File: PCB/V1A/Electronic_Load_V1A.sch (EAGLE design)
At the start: 231 parts, among them IC201 MAX743CPE, IC202 7805T, IC203 7805T, IC204 7905, IC205 LM50, IC206 LM50, IC301 OPA77P, IC401 AD620R, IC402 AD620R, IC403 AD620R, IC404 AD620R, IC405 LM50, IC406 LM50, IC407 AD620R, J101 +, J102 -, J103 +, J104 -, Q1 BC807-16SMD, Q101 SIRC10DP, Q102 SIRC10DP, Q103 SIRC10DP, Q104 IXTK102N65X2PADUP, Q105 SIRC10DP, Q106 SIRC10DP, Q107 SIRC10DP, Q108 IXTK102N65X2PADUP, Q2 BC807-16SMD, Q3 BC807-16SMD, Q301 BC817-25SMD, Q302 BC807-25SMD, Q303 BC817-25SMD, Q4 BC807-16SMD, Q5 BC807-16SMD, Q501 BC807-16SMD, Q502 BC807-16SMD, Q503 BC807-16SMD, Q504 BC807-16SMD, Q505 BC807-16SMD, Q506 BC807-16SMD, Q6 BC807-16SMD, U1 HCPL-063N, U2 HCPL-063N, U3 HCPL-063N, U301 AD420, U302 AD420, U303 LT1014, U401 LTC1865L, U402 LTC1865L, U403 LTC1865L, U404 LTC1865L, U501 HCPL-063N, U502 HCPL-063N, U503 HCPL-063N

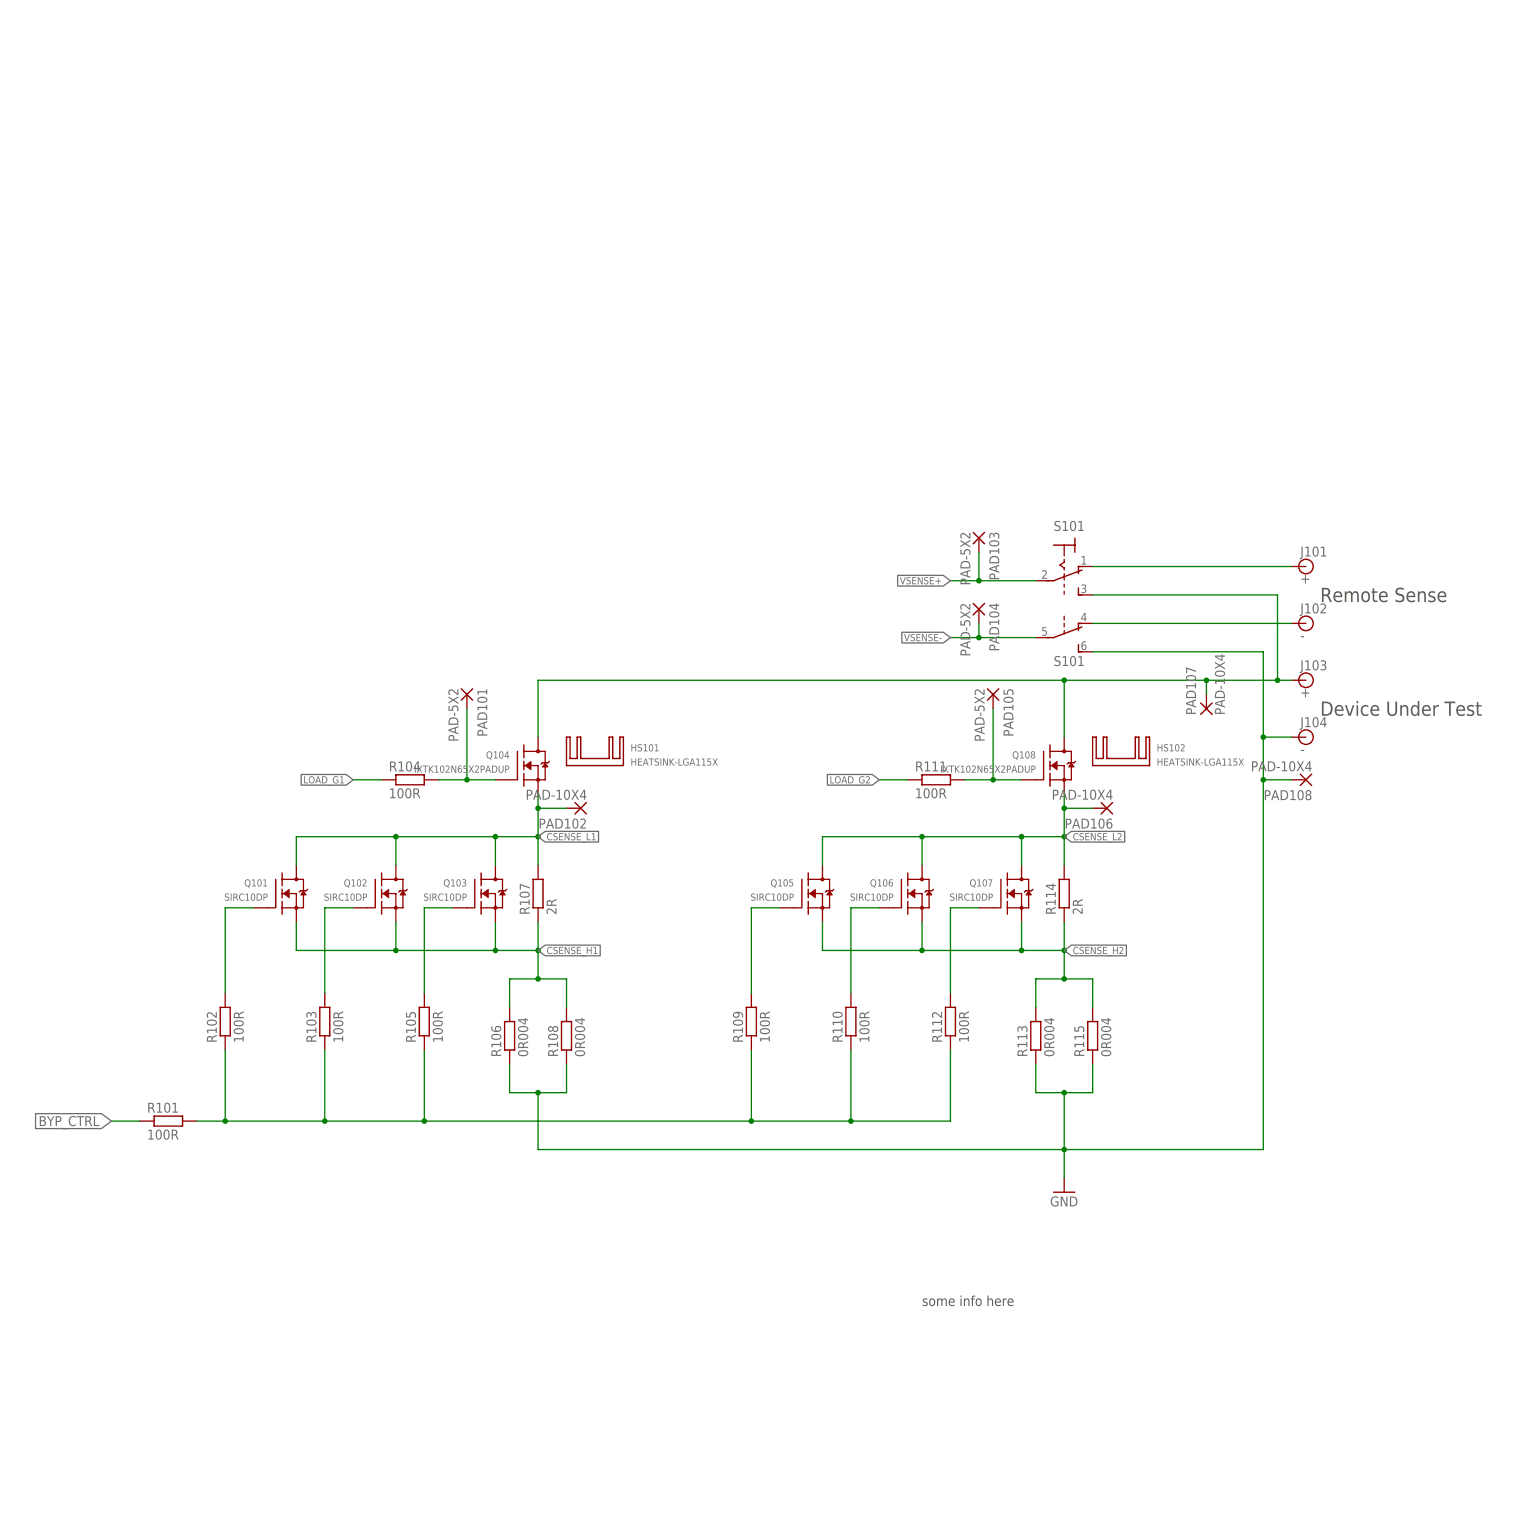
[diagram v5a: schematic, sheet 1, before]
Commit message: Removed board layout, updated schematic layout
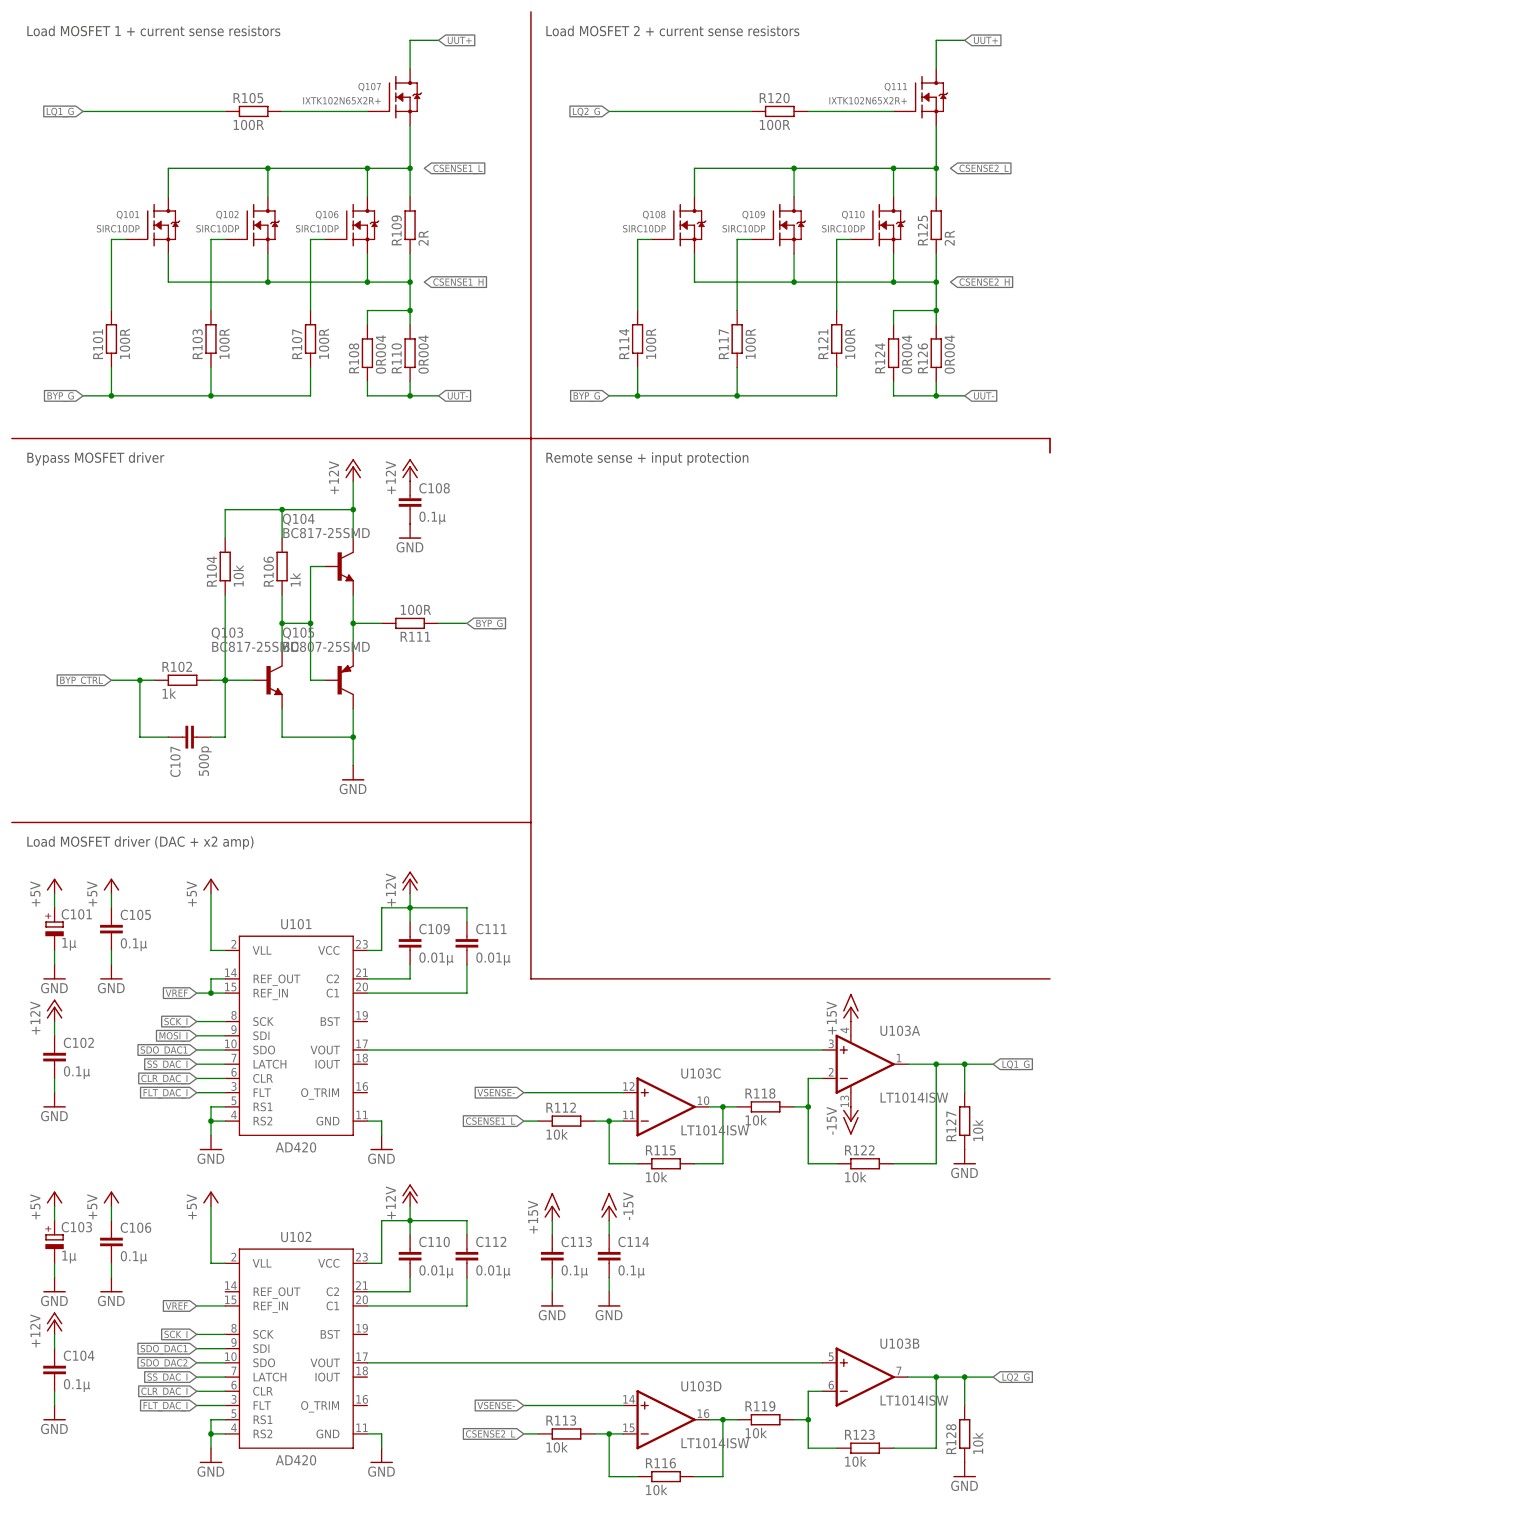
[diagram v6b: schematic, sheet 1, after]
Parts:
- removed C1, C301, C302, C303, C309, C311, C312, C5, C9: 0.1µ, rcl:C-EUC1206
- removed C10, C2, C6: 0.01µ, rcl:C-EUC1206
- removed C11, C12, C3, C4, C7, C8: 15p, rcl:C-EUC1206
- removed C13, C14, C15, C16, C308: 500p, rcl:C-EUC1206
- removed C304, C305, C306, C307: 10n, rcl:C-EUC0805
- removed C310: 0.1µ, rcl:C-EUC0805
- removed HS101, HS102: HEATSINK-LGA115X, mechanical:HEATSINK-LGA115X
- removed J101, J103: +, SparkFun-Connectors:BANANA_CONN
- removed J102, J104: -, SparkFun-Connectors:BANANA_CONN
- removed PAD101, PAD103, PAD104, PAD105: PAD-5X2, pads:PAD-5X2
- removed PAD102, PAD106, PAD107, PAD108: PAD-10X4, pads:PAD-10X4
- removed Q1, Q2, Q3, Q4, Q5, Q6: BC807-16SMD, transistor-pnp:BC807-16SMD
- removed Q301, Q303: BC817-25SMD, transistor-npn:BC817-25SMD
- removed Q302: BC807-25SMD, transistor-pnp:BC807-25SMD
- removed R1, R10, R11, R12, R2, R3, R4, R5, R6, R7, R8, R9: 350R, rcl:R-EU_R1206
- removed R13, R14, R15, R16, R309, R310: 100R, rcl:R-EU_R1206
- removed R301, R303: 1k, rcl:R-EU_R0603
- removed R302, R304: 10k, rcl:R-EU_R0603
- removed R305, R306: 20k, rcl:R-TRIMM4G/J
- removed R307, R308: 200k, rcl:R-EU_R1206
- removed R311, R312, R313, R314: 5k, rcl:R-EU_R0603
- removed S101: (no value), switch:320-938
- removed U1, U2, U3: HCPL-063N, isolation:HCPL-063N
- removed U301, U302: AD420, adc_dac:AD420
- removed U303: LT1014, SparkFun-Retired:LT1014
- added C101, C103, C426, C427: 1µ, rcl:CPOL-EUSMCA
- added C102, C104, C105, C106, C108, C113, C114, C428, C429, C513, C514, C515: 0.1µ, rcl:C-EUC1206
- added C107: 500p, rcl:C-EUC1206
- added C109, C110, C111, C112, C516, C517, C518: 0.01µ, rcl:C-EUC1206
- added C519, C520, C521, C522, C523, C524: 15p, rcl:C-EUC1206
- added Q109, Q110: SIRC10DP, transistors:SIRC10DP
- added Q111: IXTK102N65X2R+, transistors:IXTK102N65X2R+
- added Q507, Q508, Q509, Q510, Q511, Q512: BC807-16SMD, transistor-pnp:BC807-16SMD
- added R116, R118, R119, R122, R123, R127, R128: 10k, rcl:R-EU_R0603
- added R117, R120, R121: 100R, rcl:R-EU_R1206
- added R124, R126: 0R004, rcl:R-EU_R6332
- added R125: 2R, rcl:R-EU_R1206
- added R412, R413: 2M, rcl:R-EU_R1206
- added R414, R415: 2k15, rcl:R-EU_R1206
- added R513, R514, R515, R516, R517, R518, R519, R520, R521, R522, R523, R524: 350R, rcl:R-EU_R1206
- added U101, U102: AD420, adc_dac:AD420RW-24
- added U103: LT1014ISW, ic:LT1014ISW
- added U504, U505, U506: HCPL-063N, isolation:HCPL-063N
- C409, C410: value 1µ -> 500p; device rcl:CPOL-EUSMCA -> rcl:C-EUC1206
- C411, C412: value 0.1µ -> 500p
- C413, C414, C421, C422: value 0.1µ -> 1µ; device rcl:C-EUC1206 -> rcl:CPOL-EUSMCA
- C417, C418, C419, C420: value 1µ -> 0.1µ; device rcl:CPOL-EUSMCA -> rcl:C-EUC1206
- Q103: value SIRC10DP -> BC817-25SMD; device transistors:SIRC10DP -> transistor-npn:BC817-25SMD
- Q104: value IXTK102N65X2PADUP -> BC817-25SMD; device transistors:IXTK102N65X2PADUP -> transistor-npn:BC817-25SMD
- Q105: value SIRC10DP -> BC807-25SMD; device transistors:SIRC10DP -> transistor-pnp:BC807-25SMD
- Q107: value SIRC10DP -> IXTK102N65X2R+; device transistors:SIRC10DP -> transistors:IXTK102N65X2R+
- Q108: value IXTK102N65X2PADUP -> SIRC10DP; device transistors:IXTK102N65X2PADUP -> transistors:SIRC10DP
- R102: value 100R -> 1k; device rcl:R-EU_R1206 -> rcl:R-EU_R0603
- R104, R112: value 100R -> 10k; device rcl:R-EU_R1206 -> rcl:R-EU_R0603
- R106: value 0R004 -> 1k; device rcl:R-EU_R6332 -> rcl:R-EU_R0603
- R107, R114: value 2R -> 100R
- R109: value 100R -> 2R
- R110: value 100R -> 0R004; device rcl:R-EU_R1206 -> rcl:R-EU_R6332
- R113, R115: value 0R004 -> 10k; device rcl:R-EU_R6332 -> rcl:R-EU_R0603
- R405, R406, R407, R408: value 2M -> 100R
- R410, R411: value 2k15 -> 2M
- renumbered C17 to C423, C18 to C425, C19 to C424, R17 to R416, R18 to R418, R19 to R417
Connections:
- net N$56 renamed LBQ12_G
- removed net DAC1_OUT: U301.DATA_OUT, U302.DATA_IN
- removed net DAC2_OUT: U302.DATA_OUT
- removed net DUT_+1: J103.1, PAD107.P, Q104.D, Q108.D, S1011.S
- removed net LOAD_G1: R104.1, R313.2, U303G1.OUT
- removed net LOAD_G2: R111.1, R314.2, U303G2.OUT
- removed net N$24: C307.1, U302.CAP2
- removed net N$25: C304.1, U301.CAP1
- removed net N$26: C305.1, U302.CAP1
- removed net N$27: C306.1, U301.CAP2
- removed net N$28: R311.2, R313.1, U303G1.-IN
- removed net N$29: R312.2, R314.1, U303G2.-IN
- removed net N$32: R307.2, R309.2, R311.1
- removed net N$33: R305.S, R307.1
- removed net N$34: R306.S, R308.1
- removed net N$35: R308.2, R310.2, R312.1
- removed net N$52: PAD101.P, Q104.G, R104.2
- removed net N$54: PAD105.P, Q108.G, R111.2
- removed net N$55: Q103.G, R105.2
- removed net N$57: Q107.G, R112.2
- removed net N$58: Q106.G, R110.2
- removed net N$59: R101.2, R102.1, R103.1, R105.1, R109.1, R110.1, R112.1
- removed net N$60: Q101.G, R102.2
- removed net N$61: Q105.G, R109.2
- removed net N$66 (its old number): Q1.E, R3.1, U1.A1
- removed net N$67 (its old number): Q2.E, R4.1, U1.A2
- removed net N$68 (its old number): Q5.E, R11.1, U3.A1
- removed net N$69 (its old number): Q6.E, R12.1, U3.A2
- removed net N$76 (its old number): Q3.E, R7.1, U2.A1
- removed net N$77 (its old number): Q4.E, R8.1, U2.A2
- removed net N$93: Q301.B, Q302.B, Q303.C, R301.1
- removed net N$94: C303.1, Q301.C, R301.2, R302.2
- removed net N$95: C303.2, Q302.C, Q303.E
- removed net N$96: C308.1, Q303.B, R302.1, R303.2
- removed net REM_VSENSE+1: J101.1, S1011.O
- removed net REM_VSENSE-1: J102.1, S101B.O
- removed net VGATE_1: U301.VOUT, U303G1.+IN
- removed net VGATE_2: U302.VOUT, U303G2.+IN
- new net BYP_G_LOL: Q504.B
- new net CLR_DAC_I: U101.CLR, U102.CLR
- new net CSENSE1_H: Q101.S, Q102.S, Q106.S, R108.2, R109.1, R110.2
- new net CSENSE1_L: Q101.D, Q102.D, Q106.D, Q107.S, R109.2, R112.1
- new net CSENSE2_H: Q108.S, Q109.S, Q110.S, R124.2, R125.1, R126.2
- new net CSENSE2_L: Q108.D, Q109.D, Q110.D, Q111.S, R113.1, R125.2
- new net FLT_DAC_I: U101.FLT, U102.FLT
- new net LBQ11_G: Q101.G, R101.2
- new net LBQ13_G: Q106.G, R107.2
- new net LBQ21_G: Q108.G, R114.2
- new net LBQ22_G: Q109.G, R117.2
- new net LBQ23_G: Q110.G, R121.2
- new net LQ1_G: R105.1, R122.2, R127.2, U103A.OUT
- new net LQ2_G: R120.1, R123.2, R128.2, U103B.OUT
- new net MOSI_I: U101.SDI
- new net N$1: Q107.G, R105.2
- new net N$10: U101.VOUT, U103A.+IN
- new net N$11: U102.VOUT, U103B.+IN
- new net N$12: R118.2, R122.1, U103A.-IN
- new net N$13: R115.2, R118.1, U103C.OUT
- new net N$14: R112.2, R115.1, U103C.-IN
- new net N$15: R113.2, R116.1, U103D.-IN
- new net N$16: R116.2, R119.1, U103D.OUT
- new net N$2: Q111.G, R120.2
- new net N$3: C109.2, U101.C2
- new net N$4: C111.2, U101.C1
- new net N$47: Q507.E, R513.1, U504.A1
- new net N$49: Q508.E, R514.1, U505.A1
- new net N$5: Q103.C, Q104.B, Q105.B, R106.1
- new net N$6: C110.2, U102.C2
- new net N$62: Q510.E, R516.1, U504.A2
- new net N$63: Q511.E, R517.1, U505.A2
- new net N$64: Q509.E, R515.1, U506.A1
- new net N$65: Q512.E, R518.1, U506.A2
- new net N$7: C112.2, U102.C1
- new net N$8: C107.2, Q103.B, R102.2, R104.1
- new net N$9: R119.2, R123.1, U103B.-IN
- new net SCK_I: U101.SCK, U102.SCK
- new net SDO_DAC1: U101.SDO, U102.SDI
- new net SDO_DAC2: U102.SDO
- new net SS_DAC_I: U101.LATCH, U102.LATCH
- new net UUT+: Q107.D, Q111.D
- new net UUT-: R108.1, R110.1, R124.1, R126.1
- net +12V: now also C102.1, C104.1, C108.1, C109.1, C110.1, C111.1, C112.1, Q104.C, R104.2, R106.2, U101.VCC, U102.VCC; no longer C304.2, C305.2, C306.2, C307.2, C309.1, C310.1, U301.VCC, U302.VCC
- net +15V: now also C113.1, C419.1, U103A.V+; no longer C311.1, C415.1, U303G1.+V
- net +3V3: now also C413.+, C414.+, C415.1, C416.1, C426.+, C427.+, C428.1, C429.1; no longer C409.+, C410.+, C411.1, C412.1, C419.+, C420.+, C421.1, C422.1
- net +5V: now also C101.+, C103.+, C105.1, C106.1, C417.1, C418.1, C513.1, C514.1, C515.1, C516.1, C517.1, C518.1, R513.2, R514.2, R515.2, R516.2, R517.2, R518.2, R519.2, R520.2, R521.2, R522.2, R523.2, R524.2, U101.VLL, U102.VLL, U504.VCC, U505.VCC, U506.VCC; no longer C1.1, C10.1, C2.1, C301.1, C302.1, C413.1, C414.1, C5.1, C6.1, C9.1, R1.2, R10.2, R11.2, R12.2, R2.2, R3.2, R304.2, R4.2, R5.2, R6.2, R7.2, R8.2, R9.2, U1.VCC, U2.VCC, U3.VCC, U301.VLL, U302.VLL
- net +5V/1: no longer R305.E, R306.E
- net -15V: now also C114.1, C420.1, U103A.V-; no longer C312.1, C416.1, U303G1.-V
- net -5V: no longer R305.A, R306.A
- net BYP_CTRL: now also C107.1, R102.1; no longer C308.2, R101.1, R303.1
- net BYP_G: now also R101.1, R103.1, R107.1, R111.1, R114.1, R117.1, R121.1; no longer Q4.B
- net BYP_G_ISO: now also C510.1, Q104.E, Q105.E, R111.2, R510.1, U501.VO2; no longer C8.1, Q301.E, Q302.E, R6.1, U2.VO2
- net CSENSE_H1: no longer Q101.S, Q102.S, Q103.S, R106.2, R107.1, R108.2
- net CSENSE_H2: no longer Q105.S, Q106.S, Q107.S, R113.2, R114.1, R115.2
- net CSENSE_L1: no longer PAD102.P, Q101.D, Q102.D, Q103.D, Q104.S, R107.2
- net CSENSE_L2: no longer PAD106.P, Q105.D, Q106.D, Q107.D, Q108.S, R114.2
- net DAC_CLR: now also Q503.B; no longer Q5.B
- net DAC_CLR_ISO: now also C509.1, R509.1, U503.VO1; no longer C11.1, R9.1, U3.VO1
- net DAC_FAULT: now also C511.1, R511.1, U502.VO2; no longer C4.1, R2.1, U1.VO2
- net DAC_FAULT_ISO: now also Q505.B; no longer Q2.B, R304.1, U301.FAULT, U302.FAULT
- net GND: now also C101.-, C102.2, C103.-, C104.2, C105.2, C106.2, C108.2, C113.2, C114.2, C409.2, C410.2, C413.-, C414.-, C417.2, C418.2, C419.2, C420.2, C421.-, C422.-, C426.-, C427.-, C428.2, C429.2, C513.2, C514.2, C515.2, C516.2, C517.2, C518.2, C519.2, C520.2, C521.2, C522.2, C523.2, C524.2, Q103.E, Q105.C, Q507.C, Q508.C, Q509.C, Q510.C, Q511.C, Q512.C, R127.1, R128.1, R414.1, U101.GND, U101.RS1, U101.RS2, U102.GND, U102.RS1, U102.RS2, U504.C1, U504.C2, U504.GND, U505.C1, U505.C2, U505.GND, U506.C1, U506.C2, U506.GND; no longer C1.2, C10.2, C11.2, C12.2, C13.2, C14.2, C15.2, C16.2, C2.2, C3.2, C301.2, C302.2, C309.2, C310.2, C311.2, C312.2, C4.2, C409.-, C410.-, C413.2, C414.2, C417.-, C418.-, C419.-, C420.-, C421.2, C422.2, C5.2, C6.2, C7.2, C8.2, C9.2, J104.1, PAD108.P, Q1.C, Q2.C, Q3.C, Q4.C, Q5.C, Q6.C, R106.1, R108.1, R113.1, R115.1, R309.1, R310.1, R410.1, S101B.S, U1.C1, U1.C2, U1.GND, U2.C1, U2.C2, U2.GND, U3.C1, U3.C2, U3.GND, U301.GND, U301.RS1, U301.RS2, U302.GND, U302.RS1, U302.RS2
- net MISO: now also C508.1, R508.1, U502.VO1; no longer C3.1, R1.1, U1.VO1
- net MISO_ISO: now also Q502.B; no longer Q1.B
- net MOSI: now also Q510.B; no longer Q504.B, U301.DATA_IN
- net MOSI_ISO: now also C522.1, R522.1, U504.VO2; no longer C510.1, R510.1, U501.VO2
- net N$100: now also R412.1, R413.2; no longer R408.1, R409.2
- net N$101: now also R413.1, R414.2; no longer R409.1, R410.2
- net N$70: now also R405.1; no longer R13.1
- net N$71: now also Q506.B; no longer Q6.B
- net N$72: now also C409.1, R405.2; no longer C13.1, R13.2
- net N$73: now also C512.1, R512.1, U503.VO2; no longer C12.1, R10.1, U3.VO2
- net N$74: now also R406.1; no longer R14.1
- net N$75: now also C410.1, R406.2; no longer C14.1, R14.2
- net N$78: now also C411.1, R407.2; no longer C15.1, R15.2
- net N$79: now also C412.1, R408.2; no longer C16.1, R16.2
- net N$80: now also R408.1; no longer R16.1
- net N$81: now also R407.1; no longer R15.1
- net N$97: now also R409.2, R411.1; no longer R405.2, R407.1
- net N$98: now also R410.1, R411.2; no longer R406.1, R407.2
- net N$99: now also R410.2, R412.2; no longer R406.2, R408.2
- net RG1_H3: now also R415.2; no longer R411.2
- net RG2_H3: now also R415.1; no longer R411.1
- net SCK: now also Q507.B; no longer Q501.B, U301.CLOCK, U302.CLOCK
- net SCK_ISO: now also C519.1, R519.1, U504.VO1; no longer C507.1, R507.1, U501.VO1
- net SS_CH: now also Q508.B; no longer Q502.B
- net SS_CH_ISO: now also C520.1, R520.1, U505.VO1; no longer C508.1, R508.1, U502.VO1
- net SS_CL: now also Q511.B; no longer Q505.B
- net SS_CL_ISO: now also C523.1, R523.1, U505.VO2; no longer C511.1, R511.1, U502.VO2
- net SS_DAC: now also Q501.B; no longer Q3.B
- net SS_DAC_ISO: now also C507.1, R507.1, U501.VO1; no longer C7.1, R5.1, U2.VO1
- net SS_TEMP: now also Q512.B; no longer Q506.B
- net SS_TEMP_ISO: now also C524.1, R524.1, U506.VO2; no longer C512.1, R512.1, U503.VO2
- net SS_V: now also Q509.B; no longer Q503.B
- net SS_V_ISO: now also C521.1, R521.1, U506.VO1; no longer C509.1, R509.1, U503.VO1
- net TEMP1: now also C421.+; no longer C417.+
- net TEMP2: now also C422.+; no longer C418.+
- net VREF: now also U101.REF_IN, U101.REF_OUT, U102.REF_IN; no longer U301.REF_IN, U301.REF_OUT, U302.REF_IN
- net VSENSE+: now also R409.1; no longer PAD103.P, R405.1, S1011.P
- net VSENSE-: now also U103C.+IN, U103D.+IN; no longer PAD104.P, S101B.P
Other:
- note added: "Bypass MOSFET driver"
- note added: "Load MOSFET 1 + current sense resistors"
- note added: "Load MOSFET 2 + current sense resistors"
- note added: "Load MOSFET driver (DAC + x2 amp)"
- note added: "Remote sense + input protection"
- note removed: "Device Under Test"
- note removed: "Remote Sense"
- moved on the sheet: C411, C412, C415, C416, C501, C502, C503, C504, C505, C506, C507, C508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

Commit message: Schematic & layout work; added block diagram
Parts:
- removed C314, C401, C402, C403, C404, C405, C406, C407, C408, C415, C416, C417, C418, C419, C420, C428, C429, C501, C502, C503, C513, C514, C515: 0.1µ, rcl:C-EUC1206
- removed C409, C410, C411, C412, C423, C424, C425: 500p, rcl:C-EUC1206
- removed C413, C414, C421, C422, C426, C427: 1µ, rcl:CPOL-EUSMCA
- removed C504, C505, C506, C516, C517, C518: 0.01µ, rcl:C-EUC1206
- removed C507, C508, C509, C510, C511, C512, C519, C520, C521, C522, C523, C524: 15p, rcl:C-EUC1206
- removed D201, D202: 1N5817-B, diode:1N5817-B
- removed D203, D204: 1N4004, diode:1N4004
- removed IC201: MAX743CPE, maxim:MAX743CPE
- removed IC202, IC203: 7805T, linear:7805T
- removed IC204: 7905, linear:7905T
- removed IC205, IC206, IC405, IC406: LM50, linear:LM50
- removed IC401, IC402, IC403, IC404, IC407: AD620R, analog-devices:AD620R
- removed J201: (no value), con-jack:JACK-PLUG0
- removed L201, L202: 100µ, rcl:L-EU0204/5
- removed Q501, Q502, Q503, Q504, Q505, Q506, Q507, Q508, Q509, Q510, Q511, Q512: BC807-16SMD, transistor-pnp:BC807-16SMD
- removed R315, R316, R317, R318: 20k, rcl:R-EU_R0603
- removed R319: 20k, rcl:R-TRIMM4G/J
- removed R401, R402, R403, R404, R414, R415: 2k15, rcl:R-EU_R1206
- removed R405, R406, R407, R408, R416, R417, R418: 100R, rcl:R-EU_R1206
- removed R409, R410, R411, R412, R413: 2M, rcl:R-EU_R1206
- removed R501, R502, R503, R504, R505, R506, R507, R508, R509, R510, R511, R512, R513, R514, R515, R516, R517, R518, R519, R520, R521, R522, R523, R524: 350R, rcl:R-EU_R1206
- removed U401, U402, U403, U404: LTC1865L, adc_dac:LTC1865L
- removed U501, U502, U503, U504, U505, U506: HCPL-063N, isolation:HCPL-063N
- added C115, C116, C118, C217, C218, C219, C221, C301, C311, C312, C601, C602, C603, C613, C614, C615: 0.1µ, passives:C-EU-3216
- added C117, C119, C120, C220, C302: 1µ, passives:CPOL-3216-A
- added C121, C122: 500p, passives:C-EU-3216
- added C303, C305: 10n, passives:C-EU-3216
- added C304: 10µ, passives:CPOL-6032-C
- added C306, C309, C310: 220µ, rcl:CPOL-EUE3.5-10
- added C307: 0.33µ, passives:C-EU-3216
- added C308: 22µ, passives:CPOL-6032-C
- added C604, C605, C606, C616, C617, C618: 0.01µ, passives:C-EU-3216
- added C607, C608, C609, C610, C611, C612, C619, C620, C621, C622, C623, C624: 15p, passives:C-EU-3216
- added D301, D302: 1N5817-B, diode:1N5817-B
- added IC101, IC102: LM50, linear:LM50
- added IC302: OPA77P, burr-brown:OPA77P
- added J301: (no value), con-jack:JACK-PLUG0
- added L301, L302: 100µ, rcl:L-EU0204/5
- added Q601, Q602, Q603, Q604, Q605, Q606, Q607, Q608, Q609, Q610, Q611, Q612: BC807-16SMD, transistor-pnp:BC807-16SMD
- added R129: 2R, passives:R-EU-3225
- added R130: 0R004, rcl:R-EU_R6332
- added R131, R132: 10k, passives:R-EU-3225
- added R201, R202, R203, R204, R210, R211: 2k15, passives:R-EU-3225
- added R205, R206, R207, R208, R209: 2M, passives:R-EU-3225
- added R212, R213, R214, R215, R216: 100R, passives:R-EU-3225
- added R301, R302, R303, R304: 20k, passives:R-EU-3225
- added R305: 20k, rcl:R-TRIMM4G/J
- added R601, R602, R603, R604, R605, R606, R607, R608, R609, R610, R611, R612, R613, R614, R615, R616, R617, R618, R619, R620, R621, R622, R623, R624: 350R, passives:R-EU-3225
- added S201: MABSA, con-hirschmann:MABSA
- added U104: LT1014I, ic:LT1014ISW
- added U201, U202, U203, U204, U205: AD620, ic:AD620R-8
- added U206, U207, U208: LTC1865L, ic:LTC1865L
- added U301: MAX743, ic:MAX743WE
- added U601, U602, U603, U604, U605, U606: HCPL-063N, ic:HCPL-063N
- C101, C103, C215: device rcl:CPOL-EUSMCA -> passives:CPOL-3216-A
- C102, C104, C105, C106, C108, C109, C110, C111, C112, C113, C114, C202, C208, C313: device rcl:C-EUC1206 -> passives:C-EU-3216
- C201: value 220µ -> 0.1µ; device rcl:CPOL-EUE3.5-10 -> passives:C-EU-3216
- C203: value 1µ -> 0.1µ; device rcl:CPOL-EUSMCA -> passives:C-EU-3216
- C204, C206: value 10n -> 0.1µ; device rcl:C-EUC0805 -> passives:C-EU-3216
- C205: value 10µ -> 0.1µ; device rcl:CPOL-EUSMCC -> passives:C-EU-3216
- C207: value 0.33µ -> 0.1µ; device rcl:C-EUC1206 -> passives:C-EU-3216
- C209: value 22µ -> 500p; device rcl:CPOL-EUSMCD -> passives:C-EU-3216
- C210, C211: value 220µ -> 500p; device rcl:CPOL-EUE3.5-10 -> passives:C-EU-3216
- C212: value 0.33µ -> 500p; device rcl:C-EUC1206 -> passives:C-EU-3216
- C213: value 2µ2 -> 0.1µ; device rcl:CPOL-EUSMCA -> passives:C-EU-3216
- C214: value 0.1µ -> 1µ; device rcl:C-EUC1206 -> passives:CPOL-3216-A
- C216: value 0.1µ -> 500p; device rcl:C-EUC1206 -> passives:C-EU-3216
- IC301: value OPA77P -> 7805T; device burr-brown:OPA77P -> linear:7805T
- Q103, Q104: value BC817-25SMD -> BC817-16SMD; device transistor-npn:BC817-25SMD -> transistor-npn:BC817-16SMD
- Q105: value BC807-25SMD -> BC807-16SMD; device transistor-pnp:BC807-25SMD -> transistor-pnp:BC807-16SMD
- R101, R103, R105, R107, R109, R114: device rcl:R-EU_R1206 -> passives:R-EU-3225
- R102, R104, R106, R112, R113, R115, R116, R118, R127: device rcl:R-EU_R0603 -> passives:R-EU-3225
- R111, R117, R120, R121: value 100R -> 10k; device rcl:R-EU_R1206 -> passives:R-EU-3225
- R119, R122, R123: value 10k -> 100R; device rcl:R-EU_R0603 -> passives:R-EU-3225
- R124: value 0R004 -> 100R; device rcl:R-EU_R6332 -> passives:R-EU-3225
- R125: value 2R -> 100R; device rcl:R-EU_R1206 -> passives:R-EU-3225
- R126: value 0R004 -> 10k; device rcl:R-EU_R6332 -> passives:R-EU-3225
- R128: value 10k -> 0R004; device rcl:R-EU_R0603 -> rcl:R-EU_R6332
- U101, U102: device adc_dac:AD420RW-24 -> ic:AD420RW-24
- U103: value LT1014ISW -> LTC1865L; device ic:LT1014ISW -> ic:LTC1865L
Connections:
- net BYP_CTRL renamed BYP_I
- removed net +5V/1: C214.1, D203.C, IC203.VO
- removed net -5V: C215.-, C216.2, D204.A, IC204.VO
- removed net MISO_ISO: Q502.B, U401.SDO, U402.SDO, U403.SDO, U404.SDO
- removed net MOSI_ISO: C522.1, R522.1, U401.SDI, U402.SDI, U403.SDI, U404.SDI, U504.VO2
- removed net N$100: R412.1, R413.2
- removed net N$101: IC407.+, R413.1, R414.2
- removed net N$37: C206.1, IC201.CC-
- removed net N$38: C203.+, IC201.SS
- removed net N$39: D202.C, IC201.LX-, L201.1
- removed net N$40: C204.2, IC201.CC+
- removed net N$44: C207.2, C208.2, IC202.GND
- removed net N$48: IC301.+IN, R316.1, R317.2
- removed net N$50: R315.2, R317.1, R318.2
- removed net N$51: IC301.TRIM2, R319.E
- removed net N$53: IC301.TRIM1, R319.A
- removed net N$70: IC401.OUT, R405.1
- removed net N$72: C409.1, R405.2, U401.CH0
- removed net N$74: IC402.OUT, R406.1
- removed net N$75: C410.1, R406.2, U401.CH1
- removed net N$82: C423.1, R416.2, U403.CH0
- removed net N$83: C425.1, R418.2, U404.CH0
- removed net N$84: C424.1, R417.2, U403.CH1
- removed net N$97: R409.2, R411.1
- removed net N$98: R410.1, R411.2
- removed net N$99: R410.2, R412.2
- removed net RG1_H1: IC401.RG@1, R401.2
- removed net RG1_H2: IC402.RG@1, R402.2
- removed net RG1_H3: IC407.RG@1, R415.2
- removed net RG1_L1: IC403.RG@1, R403.2
- removed net RG1_L2: IC404.RG@1, R404.2
- removed net RG2_H1: IC401.RG@2, R401.1
- removed net RG2_H2: IC402.RG@2, R402.1
- removed net RG2_H3: IC407.RG@2, R415.1
- removed net RG2_L1: IC403.RG@2, R403.1
- removed net RG2_L2: IC404.RG@2, R404.1
- removed net SCK_ISO: C519.1, R519.1, U401.SCK, U402.SCK, U403.SCK, U404.SCK, U504.VO1
- removed net SS_CH_ISO: C520.1, R520.1, U401.CONV, U505.VO1
- removed net SS_CL_ISO: C523.1, R523.1, U402.CONV, U505.VO2
- removed net SS_TEMP_ISO: C524.1, R524.1, U403.CONV, U506.VO2
- removed net SS_V_ISO: C521.1, R521.1, U404.CONV, U506.VO1
- removed net VSENSE+: R409.1
- removed net VSENSE_AMP: IC407.OUT
- new net MISO_I: Q602.B, U103.SDO, U206.SDO, U207.SDO, U208.SDO
- new net N$17: R212.1, U201.OUT
- new net N$18: C209.1, R212.2, U206.CH0
- new net N$19: R213.1, U202.OUT
- new net N$20: C210.1, R213.2, U206.CH1
- new net N$21: C211.1, R214.2, U207.CH0
- new net N$22: C212.1, R215.2, U207.CH1
- new net N$23: R215.1, U204.OUT
- new net N$24: R214.1, U203.OUT
- new net N$25: R208.1, R209.2
- new net N$26: R206.2, R208.2
- new net N$27: R206.1, R207.2
- new net N$28: R205.2, R207.1
- new net N$29: R209.1, R210.2, U205.+
- new net N$30: C216.1, R216.2, U208.CH0
- new net N$31: R216.1, U205.OUT
- new net N$32: C305.1, U301.CC-
- new net N$33: C302.+, U301.SS
- new net N$34: C303.2, U301.CC+
- new net N$35: D301.A, L302.2, U301.LX+
- new net N$41: D302.C, L301.1, U301.LX-
- new net N$42: C307.2, C311.2, IC301.GND
- new net REM_SENSE+: S201.14
- new net REM_SENSE-: S201.11
- new net RG1_H4: R201.2, U201.RG@1
- new net RG1_H5: R202.2, U202.RG@1
- new net RG1_H6: R211.2, U205.RG@1
- new net RG1_L3: R203.2, U203.RG@1
- new net RG1_L4: R204.2, U204.RG@1
- new net RG2_H4: R201.1, U201.RG@2
- new net RG2_H5: R202.1, U202.RG@2
- new net RG2_H6: R211.1, U205.RG@2
- new net RG2_L3: R203.1, U203.RG@2
- new net RG2_L4: R204.1, U204.RG@2
- new net SS_CH_I: C620.1, R620.1, U206.CONV, U605.VO1
- new net SS_CL_I: C623.1, R623.1, U207.CONV, U605.VO2
- new net SS_TEMP_I: C624.1, R624.1, U103.CONV, U606.VO2
- new net SS_V_I: C621.1, R621.1, U208.CONV, U606.VO1
- new net T1_OUT: C119.+, IC101.VO, R123.1
- new net T2_OUT: C120.+, IC102.VO, R124.1
- net +12V: now also C306.+, C307.1, IC301.VI, J301.3; no longer C201.+, C207.1, IC202.VI, J201.3
- net +15V: now also C201.1, C202.1, C203.1, C204.1, C213.1, C309.+, C312.1, D301.C, IC302.V+, R305.S, U104A.V+, U201.+V, U202.+V, U203.+V, U204.+V, U205.+V, U301.FB+; no longer C210.+, C212.1, C313.1, C401.1, C402.1, C403.1, C404.1, C419.1, D201.C, IC201.FB+, IC203.VI, IC301.V+, IC401.+V, IC402.+V, IC403.+V, IC404.+V, IC407.+V, R319.S, U103A.V+
- net +3V3: now also C117.+, C118.1, C214.+, C215.+, C218.1, C219.1, C220.+, C221.1, U103.VCC, U206.VCC, U207.VCC, U208.VCC; no longer C413.+, C414.+, C415.1, C416.1, C426.+, C427.+, C428.1, C429.1, U401.VCC, U402.VCC, U403.VCC, U404.VCC
- net +5V: now also C114.1, C115.1, C301.2, C308.+, C311.1, C601.1, C602.1, C603.1, C604.1, C605.1, C606.1, C613.1, C614.1, C615.1, C616.1, C617.1, C618.1, IC101.+VS, IC102.+VS, IC301.VO, L302.1, R601.2, R602.2, R603.2, R604.2, R605.2, R606.2, R607.2, R608.2, R609.2, R610.2, R611.2, R612.2, R613.2, R614.2, R615.2, R616.2, R617.2, R618.2, R619.2, R620.2, R621.2, R622.2, R623.2, R624.2, U301.AV+, U301.V+, U301.V+@1, U301.V+@2, U301.V+@3, U601.VCC, U602.VCC, U603.VCC, U604.VCC, U605.VCC, U606.VCC; no longer C202.2, C208.1, C209.+, C417.1, C418.1, C501.1, C502.1, C503.1, C504.1, C505.1, C506.1, C513.1, C514.1, C515.1, C516.1, C517.1, C518.1, IC201.AV+, IC201.V+, IC201.V+@1, IC201.V+@2, IC201.V+@3, IC202.VO, IC205.+VS, IC206.+VS, IC405.+VS, IC406.+VS, L202.1, R501.2, R502.2, R503.2, R504.2, R505.2, R506.2, R507.2, R508.2, R509.2, R510.2, R511.2, R512.2, R513.2, R514.2, R515.2, R516.2, R517.2, R518.2, R519.2, R520.2, R521.2, R522.2, R523.2, R524.2, U501.VCC, U502.VCC, U503.VCC, U504.VCC, U505.VCC, U506.VCC
- net -15V: now also C116.1, C205.1, C206.1, C207.1, C208.1, C217.1, C310.-, C313.1, D302.A, IC302.V-, U104A.V-, U201.-V, U202.-V, U203.-V, U204.-V, U205.-V, U301.FB-; no longer C114.1, C211.-, C213.-, C314.1, C405.1, C406.1, C407.1, C408.1, C420.1, D202.A, IC201.FB-, IC204.VI, IC301.V-, IC401.-V, IC402.-V, IC403.-V, IC404.-V, IC407.-V, U103A.V-
- net BYP_G: now also Q104.E, Q105.E, R111.2, R119.1, R125.1; no longer R111.1, R117.1, R121.1
- net BYP_G_ISO: now also C610.1, R610.1, U601.VO2; no longer C510.1, Q104.E, Q105.E, R111.2, R510.1, U501.VO2
- net BYP_G_LOL: now also Q604.B; no longer Q504.B
- net CSENSE2_H: now also R128.2, R129.1, R130.2; no longer R124.2, R125.1, R126.2
- net CSENSE2_L: now also R129.2; no longer R125.2
- net CSENSE_H1: now also U201.+, U203.-; no longer IC401.+, IC403.-
- net CSENSE_H2: now also U202.+, U204.-; no longer IC402.+, IC404.-
- net CSENSE_L1: now also U203.+; no longer IC403.+
- net CSENSE_L2: now also U204.+; no longer IC404.+
- net DAC_CLR: now also Q603.B; no longer Q503.B
- net DAC_CLR_ISO: now also C609.1, R609.1, U603.VO1; no longer C509.1, R509.1, U503.VO1
- net DAC_FAULT: now also C611.1, R611.1, U602.VO2; no longer C511.1, R511.1, U502.VO2
- net DAC_FAULT_ISO: now also Q605.B; no longer Q505.B
- net GND: now also C115.2, C116.2, C117.-, C118.2, C119.-, C120.-, C121.2, C122.2, C201.2, C202.2, C203.2, C204.2, C205.2, C207.2, C208.2, C209.2, C210.2, C211.2, C213.2, C214.-, C215.-, C216.2, C217.2, C218.2, C219.2, C220.-, C221.2, C301.1, C302.-, C303.1, C304.-, C305.2, C306.-, C308.-, C309.-, C310.+, C312.2, C601.2, C602.2, C603.2, C604.2, C605.2, C606.2, C607.2, C608.2, C609.2, C610.2, C611.2, C612.2, C613.2, C614.2, C615.2, C616.2, C617.2, C618.2, C619.2, C620.2, C621.2, C622.2, C623.2, C624.2, IC101.GND, IC102.GND, J301.1, J301.2, L301.2, Q601.C, Q602.C, Q603.C, Q604.C, Q605.C, Q606.C, Q607.C, Q608.C, Q609.C, Q610.C, Q611.C, Q612.C, R111.1, R131.1, R132.1, R210.1, R301.1, R304.1, U103.GND, U201.-, U201.REF, U202.-, U202.REF, U203.REF, U204.REF, U205.REF, U206.GND, U207.GND, U208.GND, U301.12/15, U301.AGND, U301.GND, U601.C1, U601.C2, U601.GND, U602.C1, U602.C2, U602.GND, U603.C1, U603.C2, U603.GND, U604.C1, U604.C2, U604.GND, U605.C1, U605.C2, U605.GND, U606.C1, U606.C2, U606.GND; no longer C201.-, C202.1, C203.-, C204.1, C205.-, C209.-, C210.-, C211.+, C213.+, C214.2, C215.+, C216.1, C314.2, C401.2, C402.2, C403.2, C404.2, C405.2, C406.2, C407.2, C408.2, C409.2, C410.2, C411.2, C412.2, C413.-, C414.-, C415.2, C416.2, C417.2, C418.2, C419.2, C420.2, C421.-, C422.-, C423.2, C424.2, C425.2, C426.-, C427.-, C428.2, C429.2, C501.2, C502.2, C503.2, C504.2, C505.2, C506.2, C507.2, C508.2, C509.2, C510.2, C511.2, C512.2, C513.2, C514.2, C515.2, C516.2, C517.2, C518.2, C519.2, C520.2, C521.2, C522.2, C523.2, C524.2, D203.A, D204.C, IC201.12/15, IC201.AGND, IC201.GND, IC203.GND, IC204.GND, IC205.GND, IC206.GND, IC401.-, IC401.REF, IC402.-, IC402.REF, IC403.REF, IC404.REF, IC405.GND, IC406.GND, IC407.REF, J201.1, J201.2, L201.2, Q501.C, Q502.C, Q503.C, Q504.C, Q505.C, Q506.C, Q507.C, Q508.C, Q509.C, Q510.C, Q511.C, Q512.C, R127.1, R128.1, R315.1, R318.1, R414.1, U401.GND, U402.GND, U403.GND, U404.GND, U501.C1, U501.C2, U501.GND, U502.C1, U502.C2, U502.GND, U503.C1, U503.C2, U503.GND, U504.C1, U504.C2, U504.GND, U505.C1, U505.C2, U505.GND, U506.C1, U506.C2, U506.GND
- net LBQ22_G: now also R119.2; no longer R117.2
- net LBQ23_G: now also R125.2; no longer R121.2
- net LQ1_G: now also R126.2, R131.2, U104A.OUT; no longer R122.2, R127.2, U103A.OUT
- net LQ2_G: now also R122.1, R127.2, R132.2, U104B.OUT; no longer R120.1, R123.2, R128.2, U103B.OUT
- net MISO: now also C608.1, R608.1, U602.VO1; no longer C508.1, R508.1, U502.VO1
- net MOSI: now also Q609.B; no longer Q510.B
- net MOSI_I: now also C622.1, R622.1, U103.SDI, U206.SDI, U207.SDI, U208.SDI, U604.VO2
- net N$10: now also U104A.+IN; no longer U103A.+IN
- net N$11: now also U104B.+IN; no longer U103B.+IN
- net N$12: now also R120.2, R126.1, U104A.-IN; no longer R118.2, R122.1, U103A.-IN
- net N$13: now also R116.2, R120.1, U104C.OUT; no longer R118.1, U103C.OUT
- net N$14: now also R116.1, U104C.-IN; no longer U103C.-IN
- net N$15: now also R117.1, R118.1, U104D.-IN; no longer R116.1, U103D.-IN
- net N$16: now also R117.2, R118.2, R121.1, U104D.OUT; no longer R116.2, R119.1, U103D.OUT
- net N$2: now also R122.2; no longer R120.2
- net N$36: now also R205.1, S201.15; no longer D201.A, IC201.LX+, L202.2
- net N$47: now also Q612.E, R618.1, U604.A1; no longer Q507.E, R513.1, U504.A1
- net N$49: now also Q607.E, R613.1, U605.A1; no longer Q508.E, R514.1, U505.A1
- net N$62: now also Q609.E, R615.1, U604.A2; no longer Q510.E, R516.1, U504.A2
- net N$63: now also Q610.E, R616.1, U605.A2; no longer Q511.E, R517.1, U505.A2
- net N$64: now also Q608.E, R614.1, U606.A1; no longer Q509.E, R515.1, U506.A1
- net N$65: now also Q611.E, R617.1, U606.A2; no longer Q512.E, R518.1, U506.A2
- net N$66: now also Q602.E, R602.1, U602.A1; no longer Q502.E, R502.1, U502.A1
- net N$67: now also Q605.E, R605.1, U602.A2; no longer Q505.E, R505.1, U502.A2
- net N$68: now also Q603.E, R603.1, U603.A1; no longer Q503.E, R503.1, U503.A1
- net N$69: now also Q606.E, R606.1, U603.A2; no longer Q506.E, R506.1, U503.A2
- net N$71: now also Q606.B; no longer Q506.B
- net N$73: now also C612.1, R612.1, U603.VO2; no longer C512.1, R512.1, U503.VO2
- net N$76: now also Q601.E, R601.1, U601.A1; no longer Q501.E, R501.1, U501.A1
- net N$77: now also Q604.E, R604.1, U601.A2; no longer Q504.E, R504.1, U501.A2
- net N$78: now also IC302.+IN, R302.1, R303.2; no longer C411.1, R407.2, U402.CH0
- net N$79: now also R301.2, R303.1, R304.2; no longer C412.1, R408.2, U402.CH1
- net N$80: now also IC302.TRIM2, R305.E; no longer IC404.OUT, R408.1
- net N$81: now also IC302.TRIM1, R305.A; no longer IC403.OUT, R407.1
- net N$9: now also R121.2, R127.1, U104B.-IN; no longer R119.2, R123.1, U103B.-IN
- net SCK: now also Q612.B; no longer Q507.B
- net SCK_I: now also C619.1, R619.1, U103.SCK, U206.SCK, U207.SCK, U208.SCK, U604.VO1
- net SS_CH: now also Q607.B; no longer Q508.B
- net SS_CL: now also Q610.B; no longer Q511.B
- net SS_DAC: now also Q601.B; no longer Q501.B
- net SS_DAC_ISO: now also C607.1, R607.1, U601.VO1; no longer C507.1, R507.1, U501.VO1
- net SS_TEMP: now also Q611.B; no longer Q512.B
- net SS_V: now also Q608.B; no longer Q509.B
- net TEMP1: now also C121.1, R123.2, U103.CH0; no longer C421.+, IC205.VO, IC405.VO
- net TEMP2: now also C122.1, R124.2, U103.CH1; no longer C422.+, IC206.VO, IC406.VO, R417.1
- net UUT+: now also S201.16
- net UUT-: now also R128.1, R130.1, S201.13; no longer R124.1, R126.1
- net VREF: now also C304.+, R302.2, U301.VREF; no longer C205.+, IC201.VREF, R316.2
- net VREF3.0: now also IC302.-IN, IC302.OUT; no longer IC301.-IN, IC301.OUT
- net VSENSE-: now also S201.12, U104C.+IN, U104D.+IN, U205.-; no longer IC407.-, U103C.+IN, U103D.+IN
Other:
- note added: "50A range current sense"
- note added: "50mA range current sense"
- note added: "Temperature sensors"
- note added: "Voltage sense"
- note removed: "High current"
- note removed: "Low current"
- note removed: "Q1 and Q2 are the actual load MOSFETs that will dissapate most of the heat. Q3 - Q6 are used to bypass high resistance current sense resistors when load current exceeds 50mA. Current is monitored in each branch seperatly in order to protect the MOSFETs and prevent thermal runaway by actively balancing the load between them."
- note removed: "Remote sense + input protection"
- note removed: "Temperature"
- note removed: "Voltage"
- note removed: "some info here"
